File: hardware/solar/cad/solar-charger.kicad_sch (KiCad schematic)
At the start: 14 parts

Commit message: Add TODO
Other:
- note added: "TODO: Hardware current source?"
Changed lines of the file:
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@@
+    (effects (font (size 1.27 1.27)) (justify left bottom))
+  )
+  (text "TODO: Hardware current source?" (at 53.34 83.82 0)
     (effects (font (size 1.27 1.27)) (justify left bottom))
   )

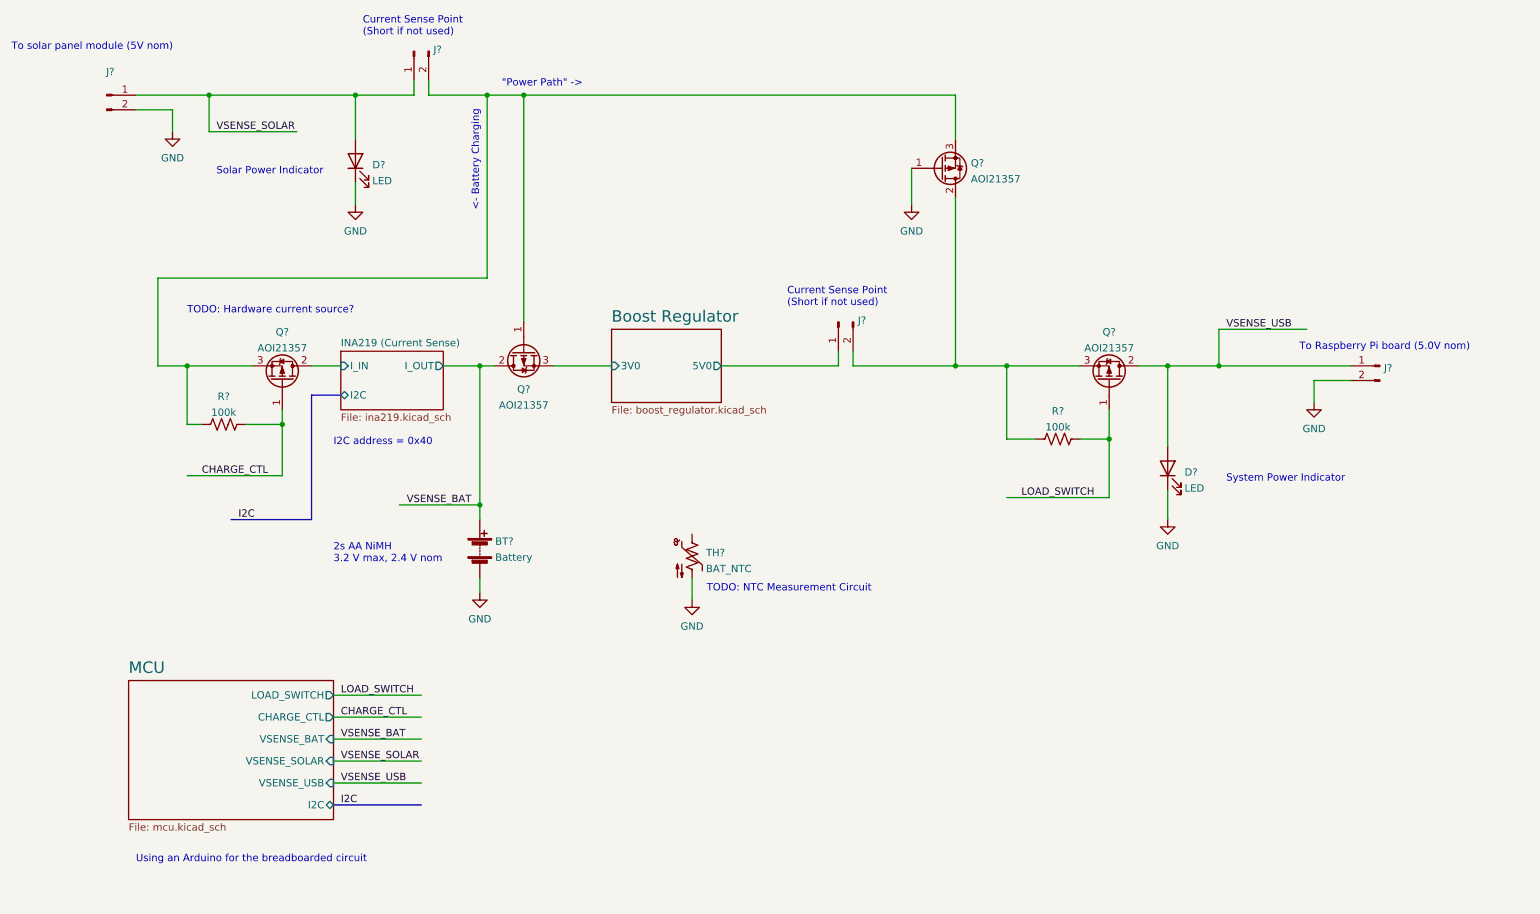
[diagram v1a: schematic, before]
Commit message: Add NTC circuit
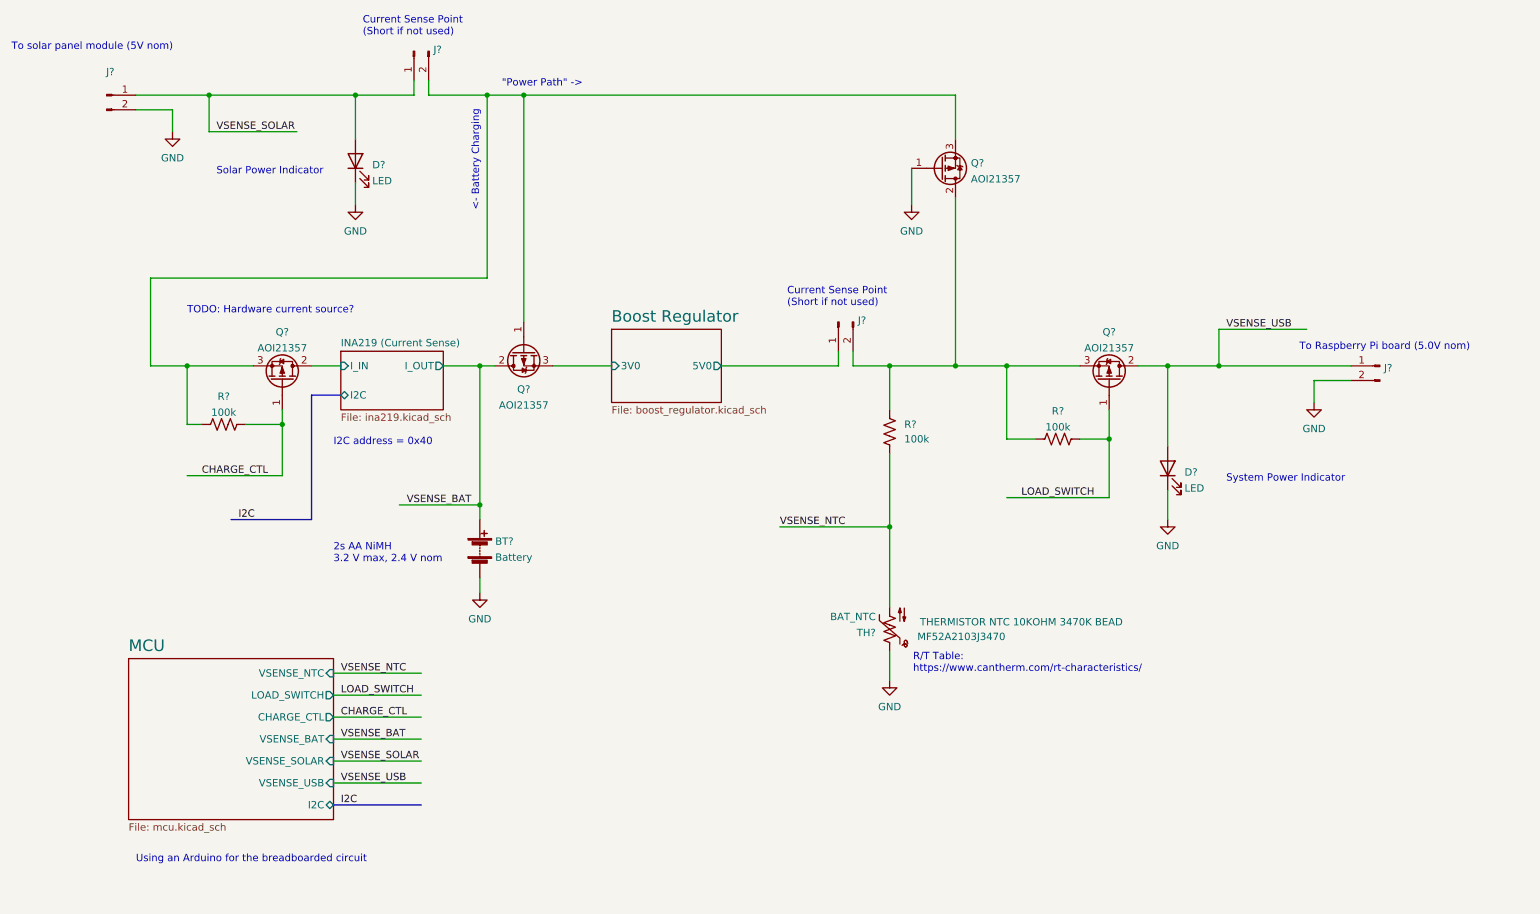
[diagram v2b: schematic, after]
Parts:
- added R?: 100k, symbol Device:R_US
- TH?: MPN (none) -> MF52A2103J3470
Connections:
- net GND: now also TH?.1; no longer TH?.2
- net at J?.2 (Pin_2), Q?.2 (D), Q?.3 (S)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: now also R?.1
- new net VSENSE_NTC: R?.2, TH?.2
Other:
- sheet MCU ports: added VSENSE_NTC; removed none
- note added: "R/T Table: https://www.cantherm.com/rt-characteristics/"
- note removed: "TODO: NTC Measurement Circuit"
- moved on the sheet: TH?
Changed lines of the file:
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@@
   (junction (at 111.76 45.72) (diameter 0) (color 0 0 0 0)
   )
+  (junction (at 175.26 120.65) (diameter 0) (color 0 0 0 0)
+  )
+  (junction (at 175.26 92.71) (diameter 0) (color 0 0 0 0)
+  )
   (junction (at 57.15 45.72) (diameter 0) (color 0 0 0 0)
   )
@@
     (stroke (width 0) (type default) (color 0 0 0 0))
   )
-  (wire (pts (xy 48.26 77.47) (xy 48.26 92.71))
+  (wire (pts (xy 46.99 77.47) (xy 46.99 92.71))
     (stroke (width 0) (type default) (color 0 0 0 0))
   )
@@
     (stroke (width 0) (type default) (color 0 0 0 0))
   )
-  (wire (pts (xy 140.97 129.54) (xy 140.97 133.35))
+  (wire (pts (xy 175.26 142.24) (xy 175.26 147.32))
     (stroke (width 0) (type default) (color 0 0 0 0))
   )
@@
     (stroke (width 0) (type default) (color 0 0 0 0))
   )
+  (wire (pts (xy 175.26 120.65) (xy 175.26 134.62))
+    (stroke (width 0) (type default) (color 0 0 0 0))
+  )
   (wire (pts (xy 218.44 92.71) (xy 223.52 92.71))
     (stroke (width 0) (type default) (color 0 0 0 0))
   )
+  (wire (pts (xy 175.26 92.71) (xy 175.26 100.33))
+    (stroke (width 0) (type default) (color 0 0 0 0))
+  )
   (wire (pts (xy 44.45 48.26) (xy 50.8 48.26))
     (stroke (width 0) (type default) (color 0 0 0 0))
@@
     (stroke (width 0) (type default) (color 0 0 0 0))
   )
+  (wire (pts (xy 175.26 92.71) (xy 186.69 92.71))
+    (stroke (width 0) (type default) (color 0 0 0 0))
+  )
   (wire (pts (xy 82.55 60.96) (xy 82.55 64.77))
     (stroke (width 0) (type default) (color 0 0 0 0))
@@
     (stroke (width 0) (type default) (color 0 0 0 0))
   )
-  (wire (pts (xy 105.41 77.47) (xy 48.26 77.47))
+  (wire (pts (xy 105.41 77.47) (xy 46.99 77.47))
     (stroke (width 0) (type default) (color 0 0 0 0))
   )
@@
     (stroke (width 0) (type default) (color 0 0 0 0))
   )
+  (wire (pts (xy 156.21 120.65) (xy 175.26 120.65))
+    (stroke (width 0) (type default) (color 0 0 0 0))
+  )
   (wire (pts (xy 105.41 45.72) (xy 105.41 77.47))
     (stroke (width 0) (type default) (color 0 0 0 0))
   )
+  (wire (pts (xy 78.74 146.05) (xy 93.98 146.05))
+    (stroke (width 0) (type default) (color 0 0 0 0))
+  )
   (wire (pts (xy 57.15 45.72) (xy 57.15 52.07))
     (stroke (width 0) (type default) (color 0 0 0 0))
@@
     (stroke (width 0) (type default) (color 0 0 0 0))
   )
-  (wire (pts (xy 168.91 92.71) (xy 186.69 92.71))
+  (wire (pts (xy 168.91 92.71) (xy 175.26 92.71))
     (stroke (width 0) (type default) (color 0 0 0 0))
   )
@@
     (stroke (width 0) (type default) (color 0 0 0 0))
   )
-  (wire (pts (xy 48.26 92.71) (xy 53.34 92.71))
+  (wire (pts (xy 46.99 92.71) (xy 53.34 92.71))
     (stroke (width 0) (type default) (color 0 0 0 0))
   )
   (bus (pts (xy 80.01 97.79) (xy 74.93 97.79))
+    (stroke (width 0) (type default) (color 0 0 0 0))
+  )
+  (wire (pts (xy 175.26 107.95) (xy 175.26 120.65))
     (stroke (width 0) (type default) (color 0 0 0 0))
   )
@@
     (effects (font (size 1.27 1.27)) (justify left bottom))
   )
+  (text "R/T Table:\nhttps://www.cantherm.com/rt-characteristics/"
+    (at 179.324 146.05 0)
+    (effects (font (size 1.27 1.27)) (justify left bottom))
+  )
   (text "2s AA NiMH\n3.2 V max, 2.4 V nom" (at 78.74 127 0)
     (effects (font (size 1.27 1.27)) (justify left bottom))
@@
     (effects (font (size 1.27 1.27)) (justify left bottom))
   )
-  (text "TODO: NTC Measurement Circuit" (at 143.51 132.08 0)
-    (effects (font (size 1.27 1.27)) (justify left bottom))
-  )
   (text "System Power Indicator" (at 233.68 113.03 0)
     (effects (font (size 1.27 1.27)) (justify left bottom))
@@
   )
   (label "I2C" (at 62.23 119.38 0)
+    (effects (font (size 1.27 1.27)) (justify left bottom))
+  )
+  (label "VSENSE_NTC" (at 156.21 120.65 0)
+    (effects (font (size 1.27 1.27)) (justify left bottom))
+  )
+  (label "VSENSE_NTC" (at 80.01 146.05 0)
     (effects (font (size 1.27 1.27)) (justify left bottom))
   )
@@
     )
     (property "Datasheet" "~" (id 3) (at 104.14 122.936 90)
+      (effects (font (size 1.27 1.27)) hide)
+    )
+    (pin "1")
+    (pin "2")
+  )
+  (symbol (lib_id "Device:R_US") (at 175.26 104.14 0) (unit 1)
+    (in_bom yes) (on_board yes) (fields_autoplaced)
+    (property "Reference" "R?" (id 0) (at 177.8 102.8699 0)
+      (effects (font (size 1.27 1.27)) (justify left))
+    )
+    (property "Value" "100k" (id 1) (at 177.8 105.4099 0)
+      (effects (font (size 1.27 1.27)) (justify left))
+    )
+    (property "Footprint" "" (id 2) (at 176.276 104.394 90)
+      (effects (font (size 1.27 1.27)) hide)
+    )
+    (property "Datasheet" "~" (id 3) (at 175.26 104.14 0)
       (effects (font (size 1.27 1.27)) hide)
     )
@@
     (pin "2")
   )
-  (symbol (lib_id "power:GND") (at 140.97 133.35 0) (unit 1)
+  (symbol (lib_id "power:GND") (at 175.26 147.32 0) (unit 1)
     (in_bom yes) (on_board yes)
-    (property "Reference" "#PWR?" (id 0) (at 140.97 139.7 0)
-      (effects (font (size 1.27 1.27)) hide)
-    )
-    (property "Value" "GND" (id 1) (at 140.97 137.9125 0))
-    (property "Footprint" "" (id 2) (at 140.97 133.35 0)
-      (effects (font (size 1.27 1.27)) hide)
-    )
-    (property "Datasheet" "" (id 3) (at 140.97 133.35 0)
+    (property "Reference" "#PWR?" (id 0) (at 175.26 153.67 0)
+      (effects (font (size 1.27 1.27)) hide)
+    )
+    (property "Value" "GND" (id 1) (at 175.26 151.8825 0))
+    (property "Footprint" "" (id 2) (at 175.26 147.32 0)
+      (effects (font (size 1.27 1.27)) hide)
+    )
+    (property "Datasheet" "" (id 3) (at 175.26 147.32 0)
       (effects (font (size 1.27 1.27)) hide)
     )
@@
     (pin "3")
   )
-  (symbol (lib_id "Device:Thermistor_NTC_US") (at 140.97 125.73 0) (unit 1)
-    (in_bom yes) (on_board yes) (fields_autoplaced)
-    (property "Reference" "TH?" (id 0) (at 143.383 125.139 0)
-      (effects (font (size 1.27 1.27)) (justify left))
-    )
-    (property "Value" "BAT_NTC" (id 1) (at 143.383 127.9141 0)
-      (effects (font (size 1.27 1.27)) (justify left))
-    )
-    (property "Footprint" "" (id 2) (at 140.97 124.46 0)
-      (effects (font (size 1.27 1.27)) hide)
-    )
-    (property "Datasheet" "~" (id 3) (at 140.97 124.46 0)
-      (effects (font (size 1.27 1.27)) hide)
-    )
+  (symbol (lib_id "Device:Thermistor_NTC_US") (at 175.26 138.43 180) (unit 1)
+    (in_bom yes) (on_board yes)
+    (property "Reference" "TH?" (id 0) (at 172.847 139.021 0)
+      (effects (font (size 1.27 1.27)) (justify left))
+    )
+    (property "Value" "BAT_NTC" (id 1) (at 172.847 136.2459 0)
+      (effects (font (size 1.27 1.27)) (justify left))
+    )
+    (property "Footprint" "" (id 2) (at 175.26 139.7 0)
+      (effects (font (size 1.27 1.27)) hide)
+    )
+    (property "Datasheet" "~" (id 3) (at 175.26 139.7 0)
+      (effects (font (size 1.27 1.27)) hide)
+    )
+    (property "MPN" "MF52A2103J3470" (id 4) (at 187.706 139.7 0))
+    (property "Description" "THERMISTOR NTC 10KOHM 3470K BEAD" (id 5) (at 198.12 137.16 0))
     (pin "1")
     (pin "2")
@@
     )
   )
-  (sheet (at 43.18 147.32) (size 35.56 24.13) (fields_autoplaced)
+  (sheet (at 43.18 143.51) (size 35.56 27.94) (fields_autoplaced)
     (stroke (width 0.1524) (type solid) (color 0 0 0 0))
     (fill (color 0 0 0 0.0000))
-    (property "Sheet name" "MCU" (id 0) (at 43.18 146.2434 0)
+    (property "Sheet name" "MCU" (id 0) (at 43.18 142.4334 0)
       (effects (font (size 2 2)) (justify left bottom))
     )
@@
     )
     (pin "I2C" bidirectional (at 78.74 168.91 0)
+      (effects (font (size 1.27 1.27)) (justify right))
+    )
+    (pin "VSENSE_NTC" input (at 78.74 146.05 0)
       (effects (font (size 1.27 1.27)) (justify right))
     )
@@
       (reference "R?") (unit 1) (value "100k") (footprint "")
     )
+    (path "/2f085b0f-8ffd-4730-997c-84fa669cb96f"
+      (reference "R?") (unit 1) (value "100k") (footprint "")
+    )

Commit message: Add op amp for current control circuit
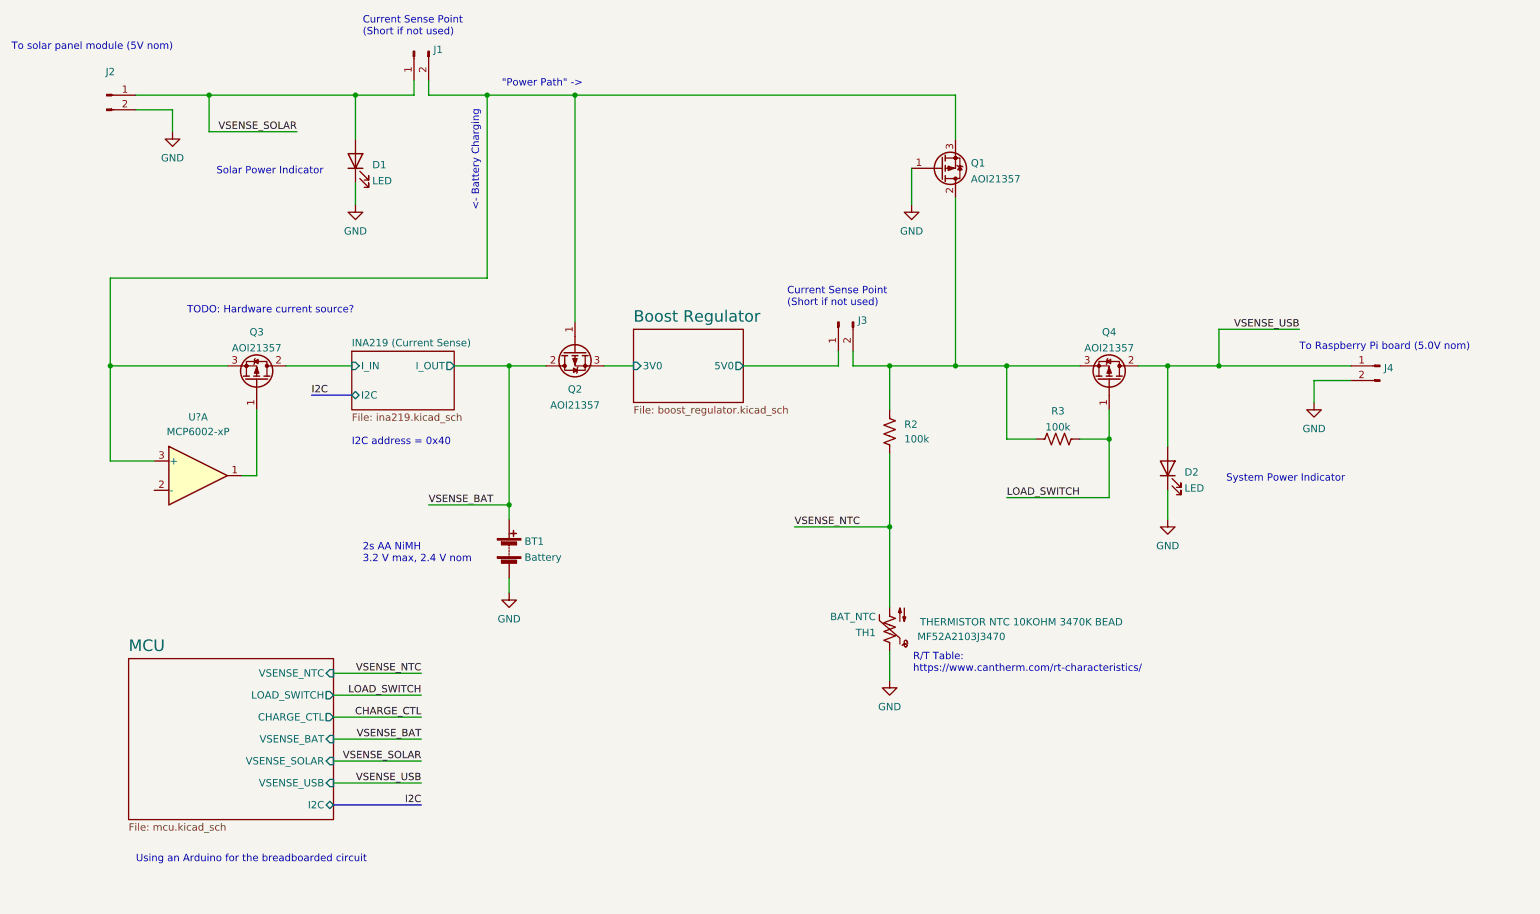
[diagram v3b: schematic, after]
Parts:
- removed R?: 100k, symbol Device:R_US
- added U?: MCP6002-xP, symbol Amplifier_Operational:MCP6002-xP
- gave numbers to parts that had none: 14
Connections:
- net CHARGE_CTL: no longer Q3.1 (G)
- net at J1.2 (Pin_2), Q1.3 (S), Q2.1 (G)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: now also U?.3 (+)
- new net: Q3.1 (G), U?.1
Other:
- moved on the sheet: BT1, Q2, Q3

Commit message: Add 200 mA (0.1C) trickle charger, neaten up schematic
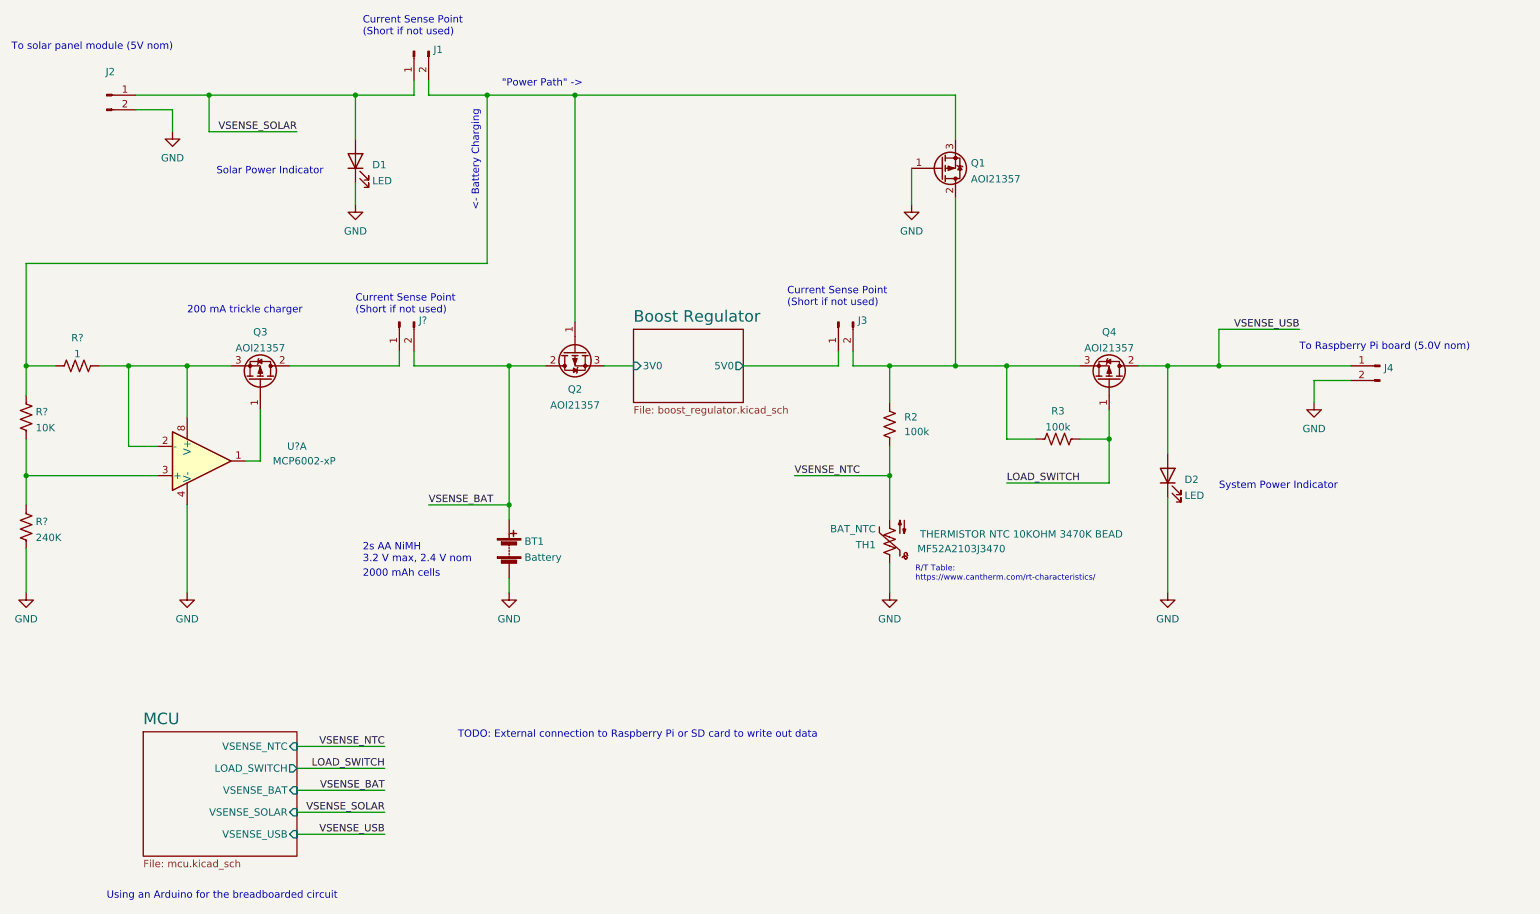
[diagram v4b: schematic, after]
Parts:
- added J?: ISENSE_SOLAR, symbol Connector:Conn_01x02_Male
- added R?: 10K, symbol Device:R_US
- added R?: 1, symbol Device:R_US
- added R?: 240K, symbol Device:R_US
- added U?: MCP6002-xP, symbol Amplifier_Operational:MCP6002-xP
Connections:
- net GND: now also R?.2, U?.4 (V-)
- net VSENSE_BAT: now also J?.2 (Pin_2)
- net at J1.2 (Pin_2), Q1.3 (S), Q2.1 (G): now also R?.1, R?.1; no longer Q3.3 (S), U?.3 (+)
- net at U?.2 (-): now also Q3.3 (S), R?.2, U?.8 (V+)
- net INA219 (Current Sense)/I_IN: no longer names the net of Q3.2 (D)
- net INA219 (Current Sense)/I_IN: now also J?.1 (Pin_1)
- new net: R?.1, R?.2, U?.3 (+)
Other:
- removed sheet INA219 (Current Sense)
- sheet MCU ports: added none; removed CHARGE_CTL, I2C
- note added: "200 mA trickle charger"
- note added: "2000 mAh cells"
- note added: "TODO: External connection to Raspberry Pi or SD card to write out data"
- note removed: "I2C address = 0x40"
- note removed: "TODO: Hardware current source?"
- moved on the sheet: D2, Q3, R2, TH1, U?A
